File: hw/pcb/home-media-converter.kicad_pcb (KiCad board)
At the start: 4 copper layers, 79.6 x 54 mm, 148 parts, among them J2 Conn_01x04_Male, J3 Conn_01x03, J4 Conn_01x03, J5 Conn_01x03, J6 RJ45_LED_Shielded, J7 USB_B, SW1 SW_Push, U1 KSZ9131RNXC-TR, U2 STM32F030F4Px, U3 DP83TG720RWRHATQ1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

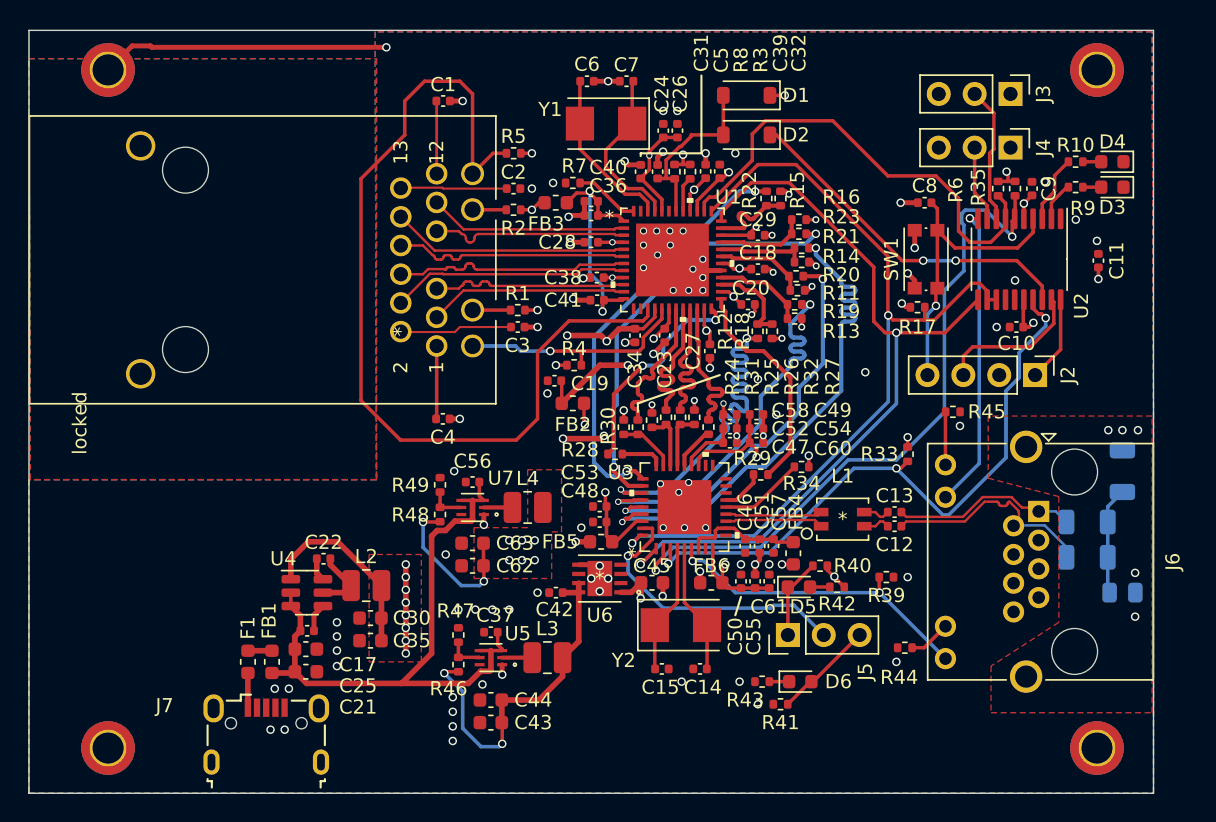
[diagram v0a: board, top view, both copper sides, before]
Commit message: Add description to silkscreen
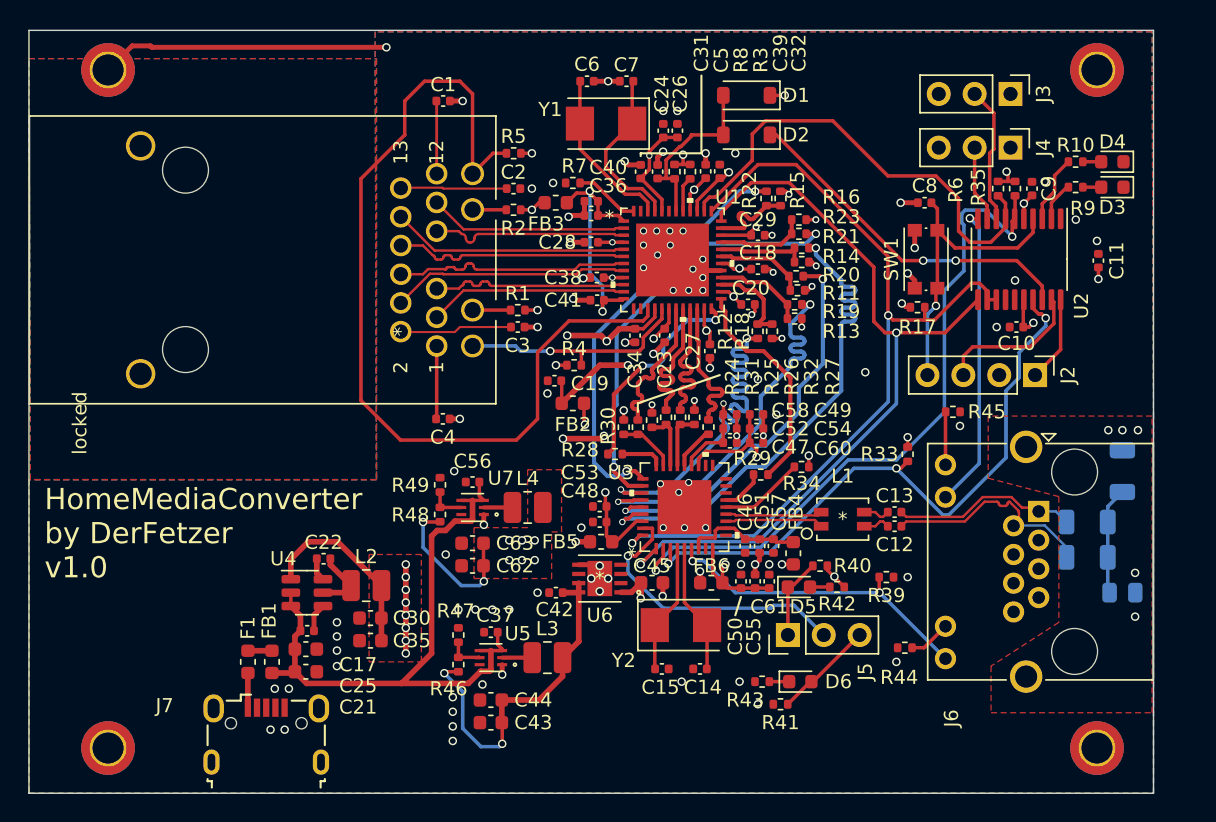
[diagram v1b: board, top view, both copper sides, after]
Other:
- board text added: "HomeMediaConverter by DerFetzer v1.0"
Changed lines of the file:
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@@
     (property "ki_keywords" "8P8C RJ socket jack connector led")
     (attr through_hole)
-    (fp_text reference "J6" (at 3.56 -9.5 -90) (layer "F.SilkS")
+    (fp_text reference "J6" (at 14.647999 6.175002 -90) (layer "F.SilkS")
         (effects (font (size 1 1) (thickness 0.15)))
     )
@@
   (gr_rect (start 33.4 104.2) (end 113 158.2)
     (stroke (width 0.1) (type default)) (fill none) (layer "Edge.Cuts"))
+  (gr_text "HomeMediaConverter\nby DerFetzer\nv1.0" (at 34.5 143.1) (layer "F.SilkS")
+    (effects (font (size 1.5 1.5) (thickness 0.15)) (justify left bottom))
+  )
   (segment (start 71.48 127.9) (end 70.7 127.9) (width 0.25) (layer "F.Cu") (net 1))
   (segment (start 76.3 125.32) (end 75.18 125.32) (width 0.4) (layer "F.Cu") (net 1))
